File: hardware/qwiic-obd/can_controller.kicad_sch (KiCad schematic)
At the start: 7 parts, among them U801 SC18IS602BIPW_128, U802 MCP2515-xST, X801 ASV-12.000MHZ-EJ-T

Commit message: Added initial layout (parts dump)
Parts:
- R801, R802, R803: footprint (none) -> Resistor_SMD:R_0805_2012Metric_Pad1.20x1.40mm_HandSolder
- U801: footprint TSSOP16_SOT403-1_NXP -> UltraLibrarian:SC18IS602BIPW_128
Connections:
- net ~{CAN_RESET} is gone; now on net ~{RESET}: U802.19 (~{RESET})
- net ~{RESET}: now reaches R802.2, U801.3 (*RESET)
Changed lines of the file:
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@@
   (junction (at 259.08 86.36) (diameter 0) (color 0 0 0 0)
+  )
+  (junction (at 182.88 86.36) (diameter 0) (color 0 0 0 0)
   )
   (junction (at 264.16 99.06) (diameter 0) (color 0 0 0 0)
@@
     (stroke (width 0) (type default) (color 0 0 0 0))
   )
+  (wire (pts (xy 176.53 86.36) (xy 182.88 86.36))
+    (stroke (width 0) (type default) (color 0 0 0 0))
+  )
   (wire (pts (xy 130.81 96.52) (xy 137.16 96.52))
     (stroke (width 0) (type default) (color 0 0 0 0))
@@
     )
   )
+  (global_label "~{RESET}" (shape input) (at 176.53 86.36 180) (fields_autoplaced)
+    (effects (font (size 1.27 1.27)) (justify right))
+    (property "Intersheet References" "${INTERSHEET_REFS}" (id 0) (at 168.3717 86.2806 0)
+      (effects (font (size 1.27 1.27)) (justify right) hide)
+    )
+  )
   (global_label "~{CAN_CS}" (shape input) (at 91.44 78.74 180) (fields_autoplaced)
     (effects (font (size 1.27 1.27)) (justify right))
@@
     )
   )
-  (global_label "~{CAN_RESET}" (shape input) (at 137.16 104.14 0) (fields_autoplaced)
-    (effects (font (size 1.27 1.27)) (justify left))
-    (property "Intersheet References" "${INTERSHEET_REFS}" (id 0) (at 149.975 104.0606 0)
+  (global_label "~{RESET}" (shape input) (at 137.16 104.14 0) (fields_autoplaced)
+    (effects (font (size 1.27 1.27)) (justify left))
+    (property "Intersheet References" "${INTERSHEET_REFS}" (id 0) (at 145.3183 104.0606 0)
       (effects (font (size 1.27 1.27)) (justify left) hide)
     )
@@
       (effects (font (size 1.27 1.27)) (justify left))
     )
-    (property "Footprint" "" (id 2) (at 262.382 77.47 90)
+    (property "Footprint" "Resistor_SMD:R_0805_2012Metric_Pad1.20x1.40mm_HandSolder" (id 2) (at 262.382 77.47 90)
       (effects (font (size 1.27 1.27)) hide)
     )
@@
       (effects (font (size 1.27 1.27)) (justify right))
     )
-    (property "Footprint" "" (id 2) (at 177.038 74.93 90)
+    (property "Footprint" "Resistor_SMD:R_0805_2012Metric_Pad1.20x1.40mm_HandSolder" (id 2) (at 177.038 74.93 90)
       (effects (font (size 1.27 1.27)) hide)
     )
@@
       (effects (font (size 1.524 1.524)))
     )
-    (property "Footprint" "TSSOP16_SOT403-1_NXP" (id 2) (at 218.44 75.184 0)
+    (property "Footprint" "UltraLibrarian:SC18IS602BIPW_128" (id 2) (at 218.44 75.184 0)
       (effects (font (size 1.524 1.524)) hide)
     )
@@
       (effects (font (size 1.27 1.27)) (justify left))
     )
-    (property "Footprint" "" (id 2) (at 181.102 74.93 90)
-      (effects (font (size 1.27 1.27)) hide)
-    )
+    (property "Footprint" "Resistor_SMD:R_0805_2012Metric_Pad1.20x1.40mm_HandSolder" (id 2) (at 181.102 74.93 90)
+      (effects (font (size 1.27 1.27)) hide)
+    )

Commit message: OK, layout v1 complete
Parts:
- removed R802, R803: 10k, Resistor_SMD:R_0805_2012Metric_Pad1.20x1.40mm_HandSolder, symbol Device:R
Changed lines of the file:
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@@
   (junction (at 259.08 86.36) (diameter 0) (color 0 0 0 0)
-  )
-  (junction (at 182.88 86.36) (diameter 0) (color 0 0 0 0)
-  )
-  (junction (at 264.16 99.06) (diameter 0) (color 0 0 0 0)
   )
   (junction (at 57.15 87.63) (diameter 0) (color 0 0 0 0)
@@
     (stroke (width 0) (type default) (color 0 0 0 0))
   )
-  (wire (pts (xy 182.88 86.36) (xy 182.88 78.74))
-    (stroke (width 0) (type default) (color 0 0 0 0))
-  )
   (wire (pts (xy 127 63.5) (xy 115.57 63.5))
     (stroke (width 0) (type default) (color 0 0 0 0))
@@
     (stroke (width 0) (type default) (color 0 0 0 0))
   )
-  (wire (pts (xy 264.16 81.28) (xy 264.16 99.06))
-    (stroke (width 0) (type default) (color 0 0 0 0))
-  )
   (wire (pts (xy 176.53 93.98) (xy 185.42 93.98))
     (stroke (width 0) (type default) (color 0 0 0 0))
@@
     (stroke (width 0) (type default) (color 0 0 0 0))
   )
-  (wire (pts (xy 264.16 68.58) (xy 264.16 73.66))
-    (stroke (width 0) (type default) (color 0 0 0 0))
-  )
   (wire (pts (xy 138.43 66.04) (xy 138.43 63.5))
     (stroke (width 0) (type default) (color 0 0 0 0))
   )
-  (wire (pts (xy 264.16 99.06) (xy 266.7 99.06))
-    (stroke (width 0) (type default) (color 0 0 0 0))
-  )
   (wire (pts (xy 57.15 104.14) (xy 57.15 107.95))
     (stroke (width 0) (type default) (color 0 0 0 0))
@@
     (stroke (width 0) (type default) (color 0 0 0 0))
   )
-  (wire (pts (xy 251.46 99.06) (xy 264.16 99.06))
-    (stroke (width 0) (type default) (color 0 0 0 0))
-  )
-  (wire (pts (xy 176.53 86.36) (xy 182.88 86.36))
+  (wire (pts (xy 251.46 99.06) (xy 266.7 99.06))
+    (stroke (width 0) (type default) (color 0 0 0 0))
+  )
+  (wire (pts (xy 176.53 86.36) (xy 185.42 86.36))
     (stroke (width 0) (type default) (color 0 0 0 0))
   )
@@
     (stroke (width 0) (type default) (color 0 0 0 0))
   )
-  (wire (pts (xy 182.88 67.31) (xy 182.88 71.12))
-    (stroke (width 0) (type default) (color 0 0 0 0))
-  )
   (wire (pts (xy 175.26 78.74) (xy 175.26 81.28))
     (stroke (width 0) (type default) (color 0 0 0 0))
   )
   (wire (pts (xy 134.62 63.5) (xy 138.43 63.5))
-    (stroke (width 0) (type default) (color 0 0 0 0))
-  )
-  (wire (pts (xy 185.42 86.36) (xy 182.88 86.36))
     (stroke (width 0) (type default) (color 0 0 0 0))
   )
@@
   (symbol (lib_id "power:+3V3") (at 255.27 73.66 0) (unit 1)
     (in_bom yes) (on_board yes) (fields_autoplaced)
-    (property "Reference" "#PWR0806" (id 0) (at 255.27 77.47 0)
+    (property "Reference" "#PWR0804" (id 0) (at 255.27 77.47 0)
       (effects (font (size 1.27 1.27)) hide)
     )
@@
     (pin "1")
   )
-  (symbol (lib_id "power:+3V3") (at 264.16 68.58 0) (unit 1)
-    (in_bom yes) (on_board yes) (fields_autoplaced)
-    (property "Reference" "#PWR0805" (id 0) (at 264.16 72.39 0)
-      (effects (font (size 1.27 1.27)) hide)
-    )
-    (property "Value" "+3V3" (id 1) (at 264.16 63.5 0))
-    (property "Footprint" "" (id 2) (at 264.16 68.58 0)
-      (effects (font (size 1.27 1.27)) hide)
-    )
-    (property "Datasheet" "" (id 3) (at 264.16 68.58 0)
-      (effects (font (size 1.27 1.27)) hide)
-    )
-    (pin "1")
-  )
   (symbol (lib_id "power:+3V3") (at 175.26 67.31 0) (unit 1)
     (in_bom yes) (on_board yes) (fields_autoplaced)
@@
   (symbol (lib_id "power:GND") (at 182.88 104.14 0) (unit 1)
     (in_bom yes) (on_board yes) (fields_autoplaced)
-    (property "Reference" "#PWR0808" (id 0) (at 182.88 110.49 0)
+    (property "Reference" "#PWR0806" (id 0) (at 182.88 110.49 0)
       (effects (font (size 1.27 1.27)) hide)
     )
@@
     (pin "1")
   )
-  (symbol (lib_id "Device:R") (at 264.16 77.47 0) (unit 1)
-    (in_bom yes) (on_board yes) (fields_autoplaced)
-    (property "Reference" "R803" (id 0) (at 266.7 76.1999 0)
-      (effects (font (size 1.27 1.27)) (justify left))
-    )
-    (property "Value" "10k" (id 1) (at 266.7 78.7399 0)
-      (effects (font (size 1.27 1.27)) (justify left))
-    )
-    (property "Footprint" "Resistor_SMD:R_0805_2012Metric_Pad1.20x1.40mm_HandSolder" (id 2) (at 262.382 77.47 90)
-      (effects (font (size 1.27 1.27)) hide)
-    )
-    (property "Datasheet" "~" (id 3) (at 264.16 77.47 0)
-      (effects (font (size 1.27 1.27)) hide)
-    )
-    (pin "1")
-    (pin "2")
-  )
   (symbol (lib_id "power:GND") (at 57.15 107.95 0) (unit 1)
     (in_bom yes) (on_board yes) (fields_autoplaced)
-    (property "Reference" "#PWR0810" (id 0) (at 57.15 114.3 0)
+    (property "Reference" "#PWR0808" (id 0) (at 57.15 114.3 0)
       (effects (font (size 1.27 1.27)) hide)
     )
@@
   (symbol (lib_id "power:+3V3") (at 57.15 85.09 0) (unit 1)
     (in_bom yes) (on_board yes) (fields_autoplaced)
-    (property "Reference" "#PWR0807" (id 0) (at 57.15 88.9 0)
+    (property "Reference" "#PWR0805" (id 0) (at 57.15 88.9 0)
       (effects (font (size 1.27 1.27)) hide)
     )
@@
   (symbol (lib_id "power:GND") (at 259.08 105.41 0) (unit 1)
     (in_bom yes) (on_board yes) (fields_autoplaced)
-    (property "Reference" "#PWR0809" (id 0) (at 259.08 111.76 0)
+    (property "Reference" "#PWR0807" (id 0) (at 259.08 111.76 0)
       (effects (font (size 1.27 1.27)) hide)
     )
@@
   (symbol (lib_id "power:GND") (at 115.57 110.49 0) (unit 1)
     (in_bom yes) (on_board yes) (fields_autoplaced)
-    (property "Reference" "#PWR0811" (id 0) (at 115.57 116.84 0)
+    (property "Reference" "#PWR0809" (id 0) (at 115.57 116.84 0)
       (effects (font (size 1.27 1.27)) hide)
     )
@@
     )
     (property "Datasheet" "" (id 3) (at 115.57 110.49 0)
-      (effects (font (size 1.27 1.27)) hide)
-    )
-    (pin "1")
-  )
-  (symbol (lib_id "power:+3V3") (at 182.88 67.31 0) (unit 1)
-    (in_bom yes) (on_board yes) (fields_autoplaced)
-    (property "Reference" "#PWR0804" (id 0) (at 182.88 71.12 0)
-      (effects (font (size 1.27 1.27)) hide)
-    )
-    (property "Value" "+3V3" (id 1) (at 182.88 62.23 0))
-    (property "Footprint" "" (id 2) (at 182.88 67.31 0)
-      (effects (font (size 1.27 1.27)) hide)
-    )
-    (property "Datasheet" "" (id 3) (at 182.88 67.31 0)
       (effects (font (size 1.27 1.27)) hide)
     )
@@
     (pin "9")
   )
-  (symbol (lib_id "Device:R") (at 182.88 74.93 0) (unit 1)
-    (in_bom yes) (on_board yes) (fields_autoplaced)
-    (property "Reference" "R802" (id 0) (at 185.42 73.6599 0)
-      (effects (font (size 1.27 1.27)) (justify left))
-    )
-    (property "Value" "10k" (id 1) (at 185.42 76.1999 0)
-      (effects (font (size 1.27 1.27)) (justify left))
-    )
-    (property "Footprint" "Resistor_SMD:R_0805_2012Metric_Pad1.20x1.40mm_HandSolder" (id 2) (at 181.102 74.93 90)
-      (effects (font (size 1.27 1.27)) hide)
-    )
-    (property "Datasheet" "~" (id 3) (at 182.88 74.93 0)
-      (effects (font (size 1.27 1.27)) hide)
-    )
-    (pin "1")
-    (pin "2")
-  )
   (symbol (lib_id "Device:C") (at 130.81 63.5 270) (unit 1)

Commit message: Fix title block
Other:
- title: Vehicle CAN Collector -> QWIIC OBDII Interface
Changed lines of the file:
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@@
   (paper "A4")
   (title_block
-    (title "Vehicle CAN Collector")
-    (date "2022-12-29")
+    (title "QWIIC OBDII Interface")
+    (date "2023-01-03")
     (rev "1")
     (company "Gavin Hurlbut")

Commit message: Shrunk layout a bit
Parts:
- X801: Digikey (none) -> 535-9309-1-ND
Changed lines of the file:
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@@
+      (effects (font (size 1.27 1.27)) hide)
+    )
+    (property "Digikey" "535-9309-1-ND" (id 4) (at 57.15 96.52 0)
       (effects (font (size 1.27 1.27)) hide)
     )

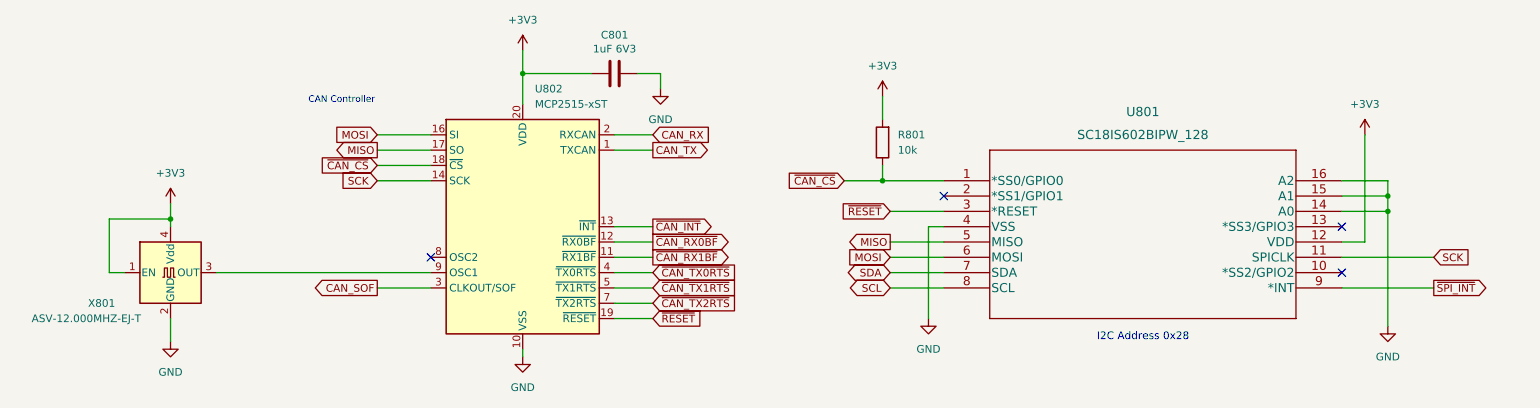
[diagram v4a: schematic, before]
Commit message: Switch out the PIC for an ATtiny424.
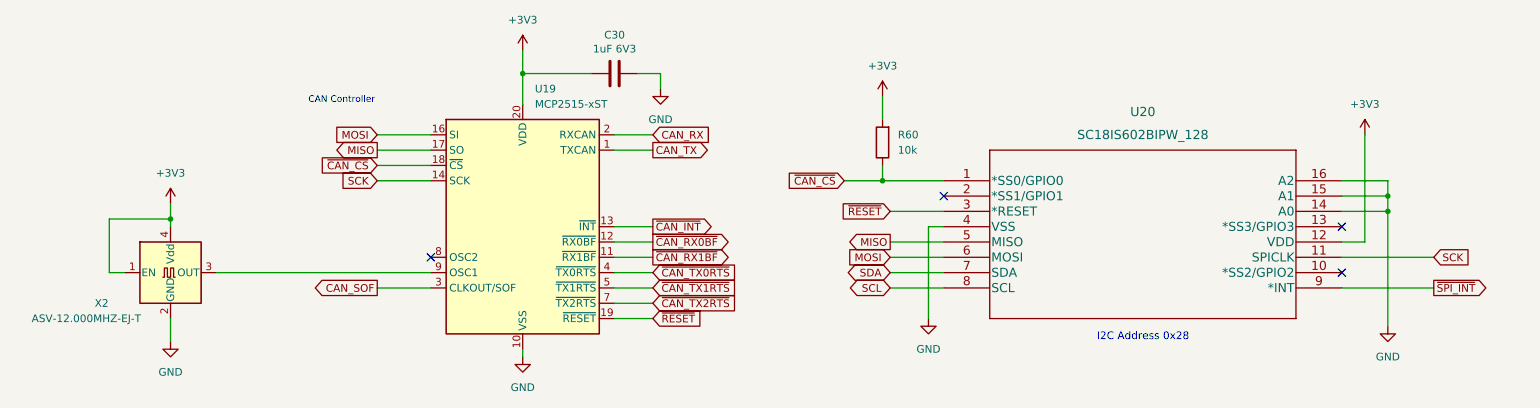
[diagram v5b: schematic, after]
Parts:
- renumbered C801 to C30, R801 to R60, U802 to U19, U801 to U20, X801 to X2
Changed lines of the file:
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@@
   (symbol (lib_id "power:+3V3") (at 255.27 73.66 0) (unit 1)
     (in_bom yes) (on_board yes) (fields_autoplaced)
-    (property "Reference" "#PWR0804" (id 0) (at 255.27 77.47 0)
+    (property "Reference" "#PWR0120" (id 0) (at 255.27 77.47 0)
       (effects (font (size 1.27 1.27)) hide)
     )
@@
   (symbol (lib_id "power:+3V3") (at 175.26 67.31 0) (unit 1)
     (in_bom yes) (on_board yes) (fields_autoplaced)
-    (property "Reference" "#PWR0803" (id 0) (at 175.26 71.12 0)
+    (property "Reference" "#PWR0118" (id 0) (at 175.26 71.12 0)
       (effects (font (size 1.27 1.27)) hide)
     )
@@
   (symbol (lib_id "power:GND") (at 182.88 104.14 0) (unit 1)
     (in_bom yes) (on_board yes) (fields_autoplaced)
-    (property "Reference" "#PWR0806" (id 0) (at 182.88 110.49 0)
+    (property "Reference" "#PWR0119" (id 0) (at 182.88 110.49 0)
       (effects (font (size 1.27 1.27)) hide)
     )
@@
   (symbol (lib_id "power:+3V3") (at 115.57 59.69 0) (unit 1)
     (in_bom yes) (on_board yes) (fields_autoplaced)
-    (property "Reference" "#PWR0801" (id 0) (at 115.57 63.5 0)
+    (property "Reference" "#PWR0115" (id 0) (at 115.57 63.5 0)
       (effects (font (size 1.27 1.27)) hide)
     )
@@
   (symbol (lib_id "power:GND") (at 57.15 107.95 0) (unit 1)
     (in_bom yes) (on_board yes) (fields_autoplaced)
-    (property "Reference" "#PWR0808" (id 0) (at 57.15 114.3 0)
+    (property "Reference" "#PWR0114" (id 0) (at 57.15 114.3 0)
       (effects (font (size 1.27 1.27)) hide)
     )
@@
   (symbol (lib_id "power:+3V3") (at 57.15 85.09 0) (unit 1)
     (in_bom yes) (on_board yes) (fields_autoplaced)
-    (property "Reference" "#PWR0805" (id 0) (at 57.15 88.9 0)
+    (property "Reference" "#PWR0113" (id 0) (at 57.15 88.9 0)
       (effects (font (size 1.27 1.27)) hide)
     )
@@
   (symbol (lib_id "Device:R") (at 175.26 74.93 180) (unit 1)
     (in_bom yes) (on_board yes) (fields_autoplaced)
-    (property "Reference" "R801" (id 0) (at 177.8 73.6599 0)
+    (property "Reference" "R60" (id 0) (at 177.8 73.6599 0)
       (effects (font (size 1.27 1.27)) (justify right))
     )
@@
   (symbol (lib_id "power:GND") (at 259.08 105.41 0) (unit 1)
     (in_bom yes) (on_board yes) (fields_autoplaced)
-    (property "Reference" "#PWR0807" (id 0) (at 259.08 111.76 0)
+    (property "Reference" "#PWR0121" (id 0) (at 259.08 111.76 0)
       (effects (font (size 1.27 1.27)) hide)
     )
@@
   (symbol (lib_id "power:GND") (at 138.43 66.04 0) (unit 1)
     (in_bom yes) (on_board yes) (fields_autoplaced)
-    (property "Reference" "#PWR0802" (id 0) (at 138.43 72.39 0)
+    (property "Reference" "#PWR0117" (id 0) (at 138.43 72.39 0)
       (effects (font (size 1.27 1.27)) hide)
     )
@@
   (symbol (lib_id "power:GND") (at 115.57 110.49 0) (unit 1)
     (in_bom yes) (on_board yes) (fields_autoplaced)
-    (property "Reference" "#PWR0809" (id 0) (at 115.57 116.84 0)
+    (property "Reference" "#PWR0116" (id 0) (at 115.57 116.84 0)
       (effects (font (size 1.27 1.27)) hide)
     )
@@
   (symbol (lib_id "Interface_CAN_LIN:MCP2515-xST") (at 115.57 88.9 0) (unit 1)
     (in_bom yes) (on_board yes) (fields_autoplaced)
-    (property "Reference" "U802" (id 0) (at 117.5894 66.04 0)
+    (property "Reference" "U19" (id 0) (at 117.5894 66.04 0)
       (effects (font (size 1.27 1.27)) (justify left))
     )
@@
   (symbol (lib_id "UltraLibrarian:SC18IS602BIPW_128") (at 185.42 81.28 0) (unit 1)
     (in_bom yes) (on_board yes) (fields_autoplaced)
-    (property "Reference" "U801" (id 0) (at 218.44 69.85 0)
+    (property "Reference" "U20" (id 0) (at 218.44 69.85 0)
       (effects (font (size 1.524 1.524)))
     )
@@
   (symbol (lib_id "Device:C") (at 130.81 63.5 270) (unit 1)
     (in_bom yes) (on_board yes)
-    (property "Reference" "C801" (id 0) (at 130.81 57.0992 90))
+    (property "Reference" "C30" (id 0) (at 130.81 57.0992 90))
     (property "Value" "1uF 6V3" (id 1) (at 130.81 59.4106 90))
     (property "Footprint" "Capacitor_SMD:C_0805_2012Metric_Pad1.18x1.45mm_HandSolder" (id 2) (at 127 64.4652 0)
@@
   (symbol (lib_id "Oscillator:ASV-xxxMHz") (at 57.15 96.52 0) (unit 1)
     (in_bom yes) (on_board yes)
-    (property "Reference" "X801" (id 0) (at 45.72 101.6 0))
+    (property "Reference" "X2" (id 0) (at 45.72 101.6 0))
     (property "Value" "ASV-12.000MHZ-EJ-T" (id 1) (at 43.18 104.14 0))
     (property "Footprint" "Oscillator:Oscillator_SMD_Abracon_ASV-4Pin_7.0x5.1mm" (id 2) (at 74.93 105.41 0)
